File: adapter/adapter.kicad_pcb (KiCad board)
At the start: 2 copper layers, 61 x 25.4 mm, 4 parts, among them J1 FlipperGPIO, U1 CC1101_Connector

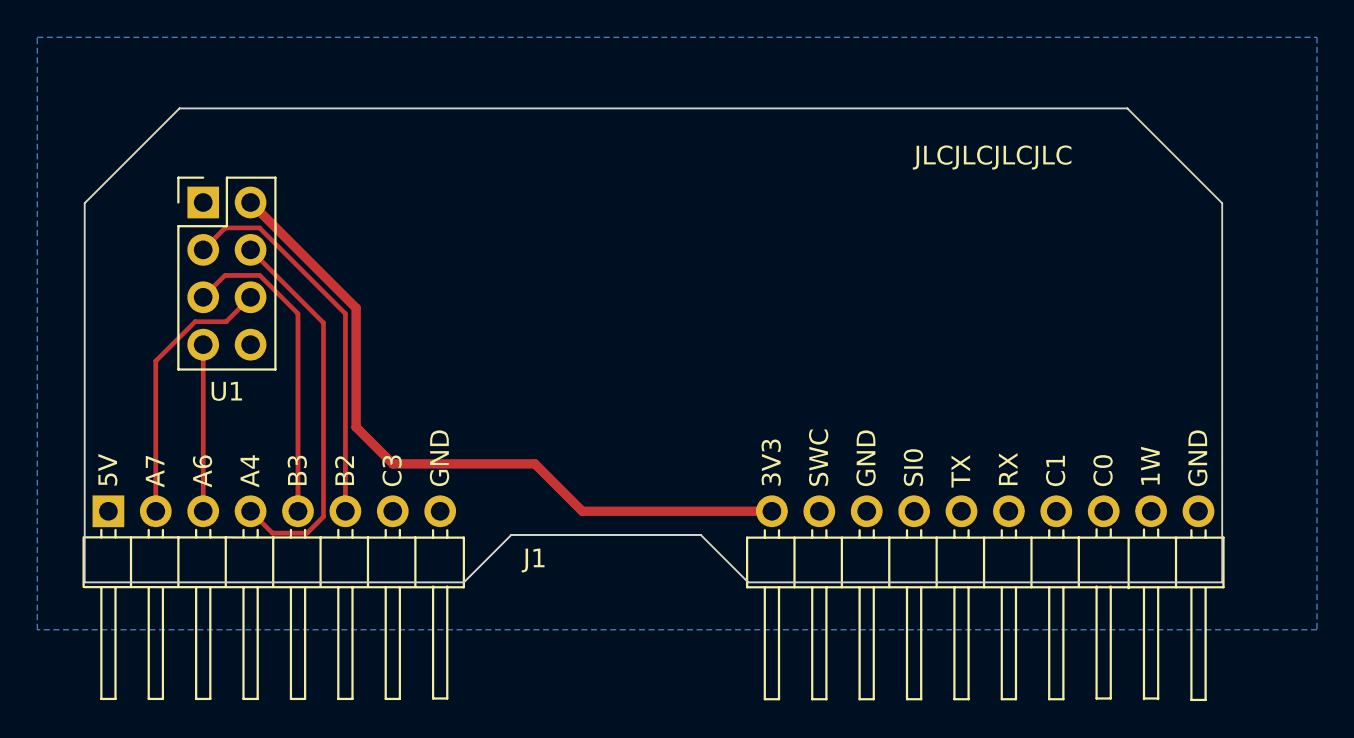
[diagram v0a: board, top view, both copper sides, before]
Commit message: include a 5V to 3.3V buck converter for more reliable power supply update to include a power LED since 5V is not always active
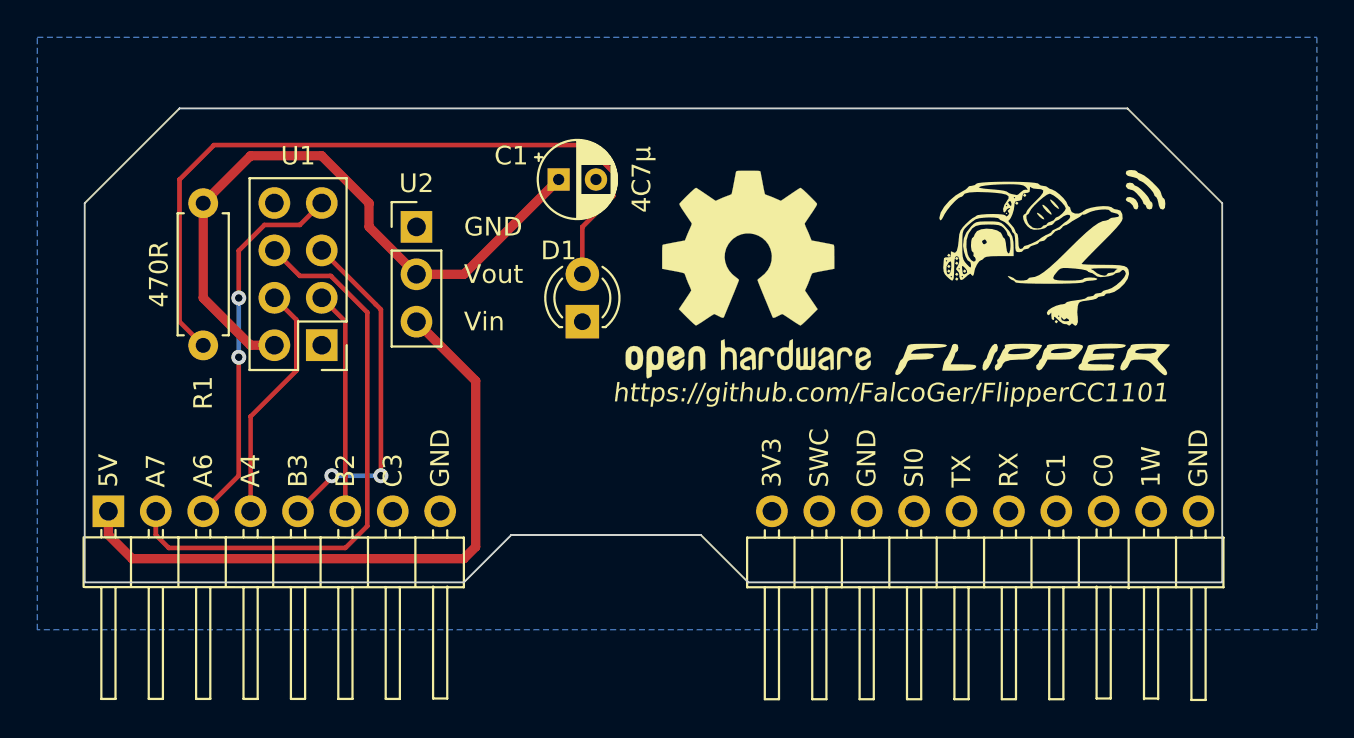
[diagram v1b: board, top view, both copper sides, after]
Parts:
- added C1: 4C7µ, Capacitor_THT:CP_Radial_D4.0mm_P2.00mm, F.Cu at (120.7, 83.8)
- added D1: LED, LED_THT:LED_D3.0mm, F.Cu at (121.9, 91.4)
- added R1: 470R, Resistor_THT:R_Axial_DIN0207_L6.3mm_D2.5mm_P7.62mm_Horizontal, F.Cu at (101.6, 85.1)
- added U2: AMS1117-3.3, Connector_PinHeader_2.54mm:PinHeader_1x03_P2.54mm_Vertical, F.Cu at (113.0, 86.4)
- REF** (x2): moved to F.Cu
- moved REF** 16.5 mm to (130.8, 88.9), turned to 0 degrees
- moved U1 9.94 mm to (108.0, 92.7), turned to 180 degrees
- moved REF** 8.89 mm to (146.1, 81.2), turned to 0 degrees
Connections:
- J1 pad 1: unconnected-(J1-Pad1) -> /5V
- J1 pad 5: /GDO0 -> /SCK
- J1 pad 6: Net-(U1-Pad3) -> /GDO0
- J1 pad 9: /3V3 -> unconnected-(J1-Pad9)
- U1 pad 3: Net-(U1-Pad3) -> /GDO0
- U1 pad 5: /GDO0 -> /SCK
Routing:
- net Net-(D1-Pad2): track 0.00 -> 40.2 mm
- net /5V: track 0.00 -> 35.1 mm
- net Net-(U1-Pad3): track 20.6 -> 0.00 mm
- net /SCK: track 0.00 -> 18.7 mm, vias 0 -> 2
- net /MOSI: track 14.5 -> 31.2 mm
- net /MISO: track 8.93 -> 20.3 mm, vias 0 -> 2
- net /CSN: track 20.7 -> 12.9 mm
- net /GDO0: track 17.0 -> 12.0 mm
- net /3V3: track 38.5 -> 35.5 mm
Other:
- board text added: "GND"
- board text added: "Vin"
- board text added: "Vout"

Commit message: rearranged board layout to make space for the buck converter
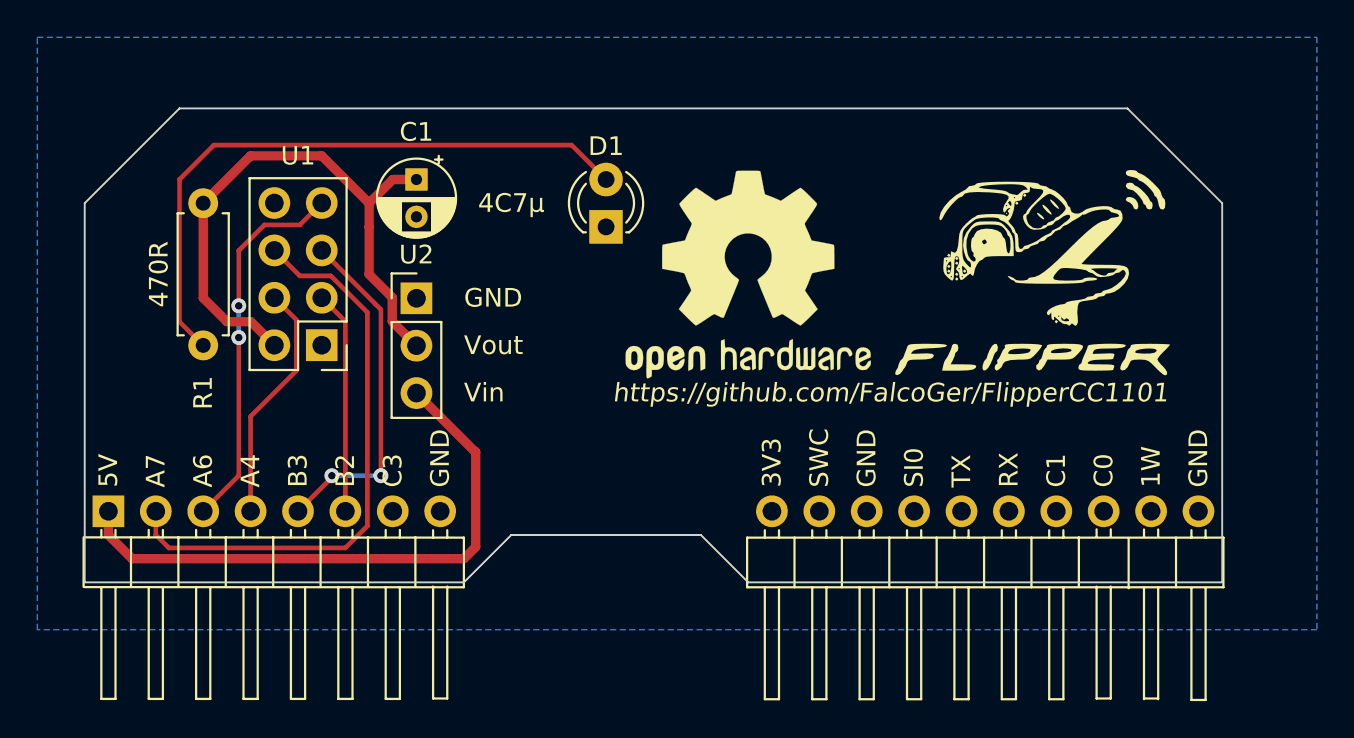
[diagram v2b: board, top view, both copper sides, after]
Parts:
- moved C1 7.62 mm to (113.0, 83.8), turned to -90 degrees
- moved D1 5.24 mm to (123.2, 86.4)
- moved U2 3.83 mm to (113.0, 90.2)
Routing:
- net Net-(D1-Pad2): track 40.2 -> 33.8 mm
- net /5V: track 35.1 -> 31.3 mm
- net /3V3: track 35.5 -> 32.7 mm
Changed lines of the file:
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@@
   )
   (footprint "Connector_PinHeader_2.54mm:PinHeader_1x03_P2.54mm_Vertical" (layer "F.Cu")
-    (at 113.03 86.36)
+    (at 113.03 90.185)
     (descr "Through hole straight pin header, 1x03, 2.54mm pitch, single row")
     (tags "Through hole pin header THT 1x03 2.54mm single row")
@@
   )
   (footprint "Capacitor_THT:CP_Radial_D4.0mm_P2.00mm" (layer "F.Cu")
-    (at 120.65 83.82)
+    (at 113.03 83.82 -90)
     (descr "CP, Radial series, Radial, pin pitch=2.00mm, , diameter=4mm, Electrolytic Capacitor")
     (tags "CP Radial series Radial pin pitch 2.00mm  diameter 4mm Electrolytic Capacitor")
@@
     (property "Sheetname" "")
     (attr through_hole)
-    (fp_text reference "C1" (at -2.54 -1.27) (layer "F.SilkS")
+    (fp_text reference "C1" (at -2.54 0 180) (layer "F.SilkS")
       (effects (font (size 1 1) (thickness 0.15)))
     )
-    (fp_text value "4C7µ" (at 4.445 0 90) (layer "F.SilkS")
+    (fp_text value "4C7µ" (at 1.27 -5.08) (layer "F.SilkS")
       (effects (font (size 1 1) (thickness 0.15)))
     )
-    (fp_text user "${REFERENCE}" (at 1 0) (layer "F.Fab")
+    (fp_text user "${REFERENCE}" (at 1 0 90) (layer "F.Fab")
       (effects (font (size 0.8 0.8) (thickness 0.12)))
     )
@@
     (fp_line (start -0.702554 -0.8675) (end -0.302554 -0.8675) (layer "F.Fab") (width 0.1))
     (fp_circle (center 1 0) (end 3 0) (layer "F.Fab") (width 0.1) (fill none))
-    (pad "1" thru_hole rect (at 0 0) (size 1.2 1.2) (drill 0.6) (layers *.Cu *.Mask)
+    (pad "1" thru_hole rect (at 0 0 270) (size 1.2 1.2) (drill 0.6) (layers *.Cu *.Mask)
       (net 17 "/3V3") (pintype "passive"))
-    (pad "2" thru_hole circle (at 2 0) (size 1.2 1.2) (drill 0.6) (layers *.Cu *.Mask)
+    (pad "2" thru_hole circle (at 2 0 270) (size 1.2 1.2) (drill 0.6) (layers *.Cu *.Mask)
       (net 16 "/GND") (pintype "passive"))
     (model "${KICAD6_3DMODEL_DIR}/Capacitor_THT.3dshapes/CP_Radial_D4.0mm_P2.00mm.wrl"
@@
   )
   (footprint "LED_THT:LED_D3.0mm" (layer "F.Cu")
-    (at 121.92 91.44 90)
+    (at 123.19 86.36 90)
     (descr "LED, diameter 3.0mm, 2 pins")
     (tags "LED diameter 3.0mm 2 pins")
@@
     (property "Sheetname" "")
     (attr through_hole)
-    (fp_text reference "D1" (at 3.81 -1.27 180) (layer "F.SilkS")
+    (fp_text reference "D1" (at 4.318 0 180) (layer "F.SilkS")
       (effects (font (size 1 1) (thickness 0.15)))
     )
@@
     (effects (font (size 1 1) (thickness 0.15)) (justify left mirror))
   )
-  (gr_text "GND" (at 115.57 86.36) (layer "F.SilkS")
+  (gr_text "GND" (at 115.57 90.17) (layer "F.SilkS")
     (effects (font (size 1 1) (thickness 0.15)) (justify left))
   )
-  (gr_text "Vout" (at 115.57 88.9) (layer "F.SilkS")
+  (gr_text "Vout" (at 115.57 92.71) (layer "F.SilkS")
     (effects (font (size 1 1) (thickness 0.15)) (justify left))
   )
@@
     (effects (font (size 1 1) (thickness 0.15) italic))
   )
-  (gr_text "Vin" (at 115.57 91.44) (layer "F.SilkS")
+  (gr_text "Vin" (at 115.57 95.25) (layer "F.SilkS")
     (effects (font (size 1 1) (thickness 0.15)) (justify left))
   )
-  (segment (start 121.92 88.9) (end 121.92 86.36) (width 0.25) (layer "F.Cu") (net 1))
+  (segment (start 121.345481 81.975481) (end 102.174519 81.975481) (width 0.25) (layer "F.Cu") (net 1))
+  (segment (start 100.33 83.82) (end 100.33 91.44) (width 0.25) (layer "F.Cu") (net 1))
   (segment (start 102.174519 81.975481) (end 100.33 83.82) (width 0.25) (layer "F.Cu") (net 1))
-  (segment (start 121.92 86.36) (end 123.574511 84.705489) (width 0.25) (layer "F.Cu") (net 1))
-  (segment (start 123.574511 84.705489) (end 123.574511 83.437054) (width 0.25) (layer "F.Cu") (net 1))
-  (segment (start 123.574511 83.437054) (end 122.112938 81.975481) (width 0.25) (layer "F.Cu") (net 1))
-  (segment (start 100.33 83.82) (end 100.33 91.44) (width 0.25) (layer "F.Cu") (net 1))
+  (segment (start 123.19 83.82) (end 121.345481 81.975481) (width 0.25) (layer "F.Cu") (net 1))
   (segment (start 100.33 91.44) (end 101.6 92.71) (width 0.25) (layer "F.Cu") (net 1))
-  (segment (start 122.112938 81.975481) (end 102.174519 81.975481) (width 0.25) (layer "F.Cu") (net 1))
-  (segment (start 116.205 94.615) (end 113.03 91.44) (width 0.5) (layer "F.Cu") (net 2))
   (segment (start 97.79 104.14) (end 115.57 104.14) (width 0.5) (layer "F.Cu") (net 2))
   (segment (start 96.52 101.6) (end 96.52 102.87) (width 0.5) (layer "F.Cu") (net 2))
+  (segment (start 116.205 103.505) (end 116.205 98.425) (width 0.5) (layer "F.Cu") (net 2))
   (segment (start 96.52 102.87) (end 97.79 104.14) (width 0.5) (layer "F.Cu") (net 2))
   (segment (start 115.57 104.14) (end 116.205 103.505) (width 0.5) (layer "F.Cu") (net 2))
-  (segment (start 116.205 103.505) (end 116.205 94.615) (width 0.5) (layer "F.Cu") (net 2))
+  (segment (start 116.19 98.425) (end 116.205 98.425) (width 0.5) (layer "F.Cu") (net 2))
+  (segment (start 113.03 95.265) (end 116.19 98.425) (width 0.5) (layer "F.Cu") (net 2))
   (segment (start 99.06 102.87) (end 99.06 101.6) (width 0.25) (layer "F.Cu") (net 12))
   (segment (start 110.394511 90.938501) (end 110.394511 102.390969) (width 0.25) (layer "F.Cu") (net 12))
@@
   (segment (start 110.394511 102.390969) (end 109.22 103.56548) (width 0.25) (layer "F.Cu") (net 12))
   (segment (start 109.22 103.56548) (end 99.75548 103.56548) (width 0.25) (layer "F.Cu") (net 12))
-  (segment (start 103.505 93.345) (end 103.505 99.695) (width 0.25) (layer "F.Cu") (net 13))
   (segment (start 103.505 99.695) (end 101.6 101.6) (width 0.25) (layer "F.Cu") (net 13))
   (segment (start 107.955 85.08) (end 106.780489 86.254511) (width 0.25) (layer "F.Cu") (net 13))
   (segment (start 106.780489 86.254511) (end 104.880489 86.254511) (width 0.25) (layer "F.Cu") (net 13))
-  (segment (start 103.505 87.63) (end 103.505 90.17) (width 0.25) (layer "F.Cu") (net 13))
+  (segment (start 103.505 92.2895) (end 103.505 99.695) (width 0.25) (layer "F.Cu") (net 13))
+  (segment (start 103.505 87.63) (end 103.505 90.5905) (width 0.25) (layer "F.Cu") (net 13))
   (segment (start 104.880489 86.254511) (end 103.505 87.63) (width 0.25) (layer "F.Cu") (net 13))
-  (via (at 103.505 93.345) (size 0.8) (drill 0.4) (layers "F.Cu" "B.Cu") (net 13))
-  (via (at 103.505 90.17) (size 0.8) (drill 0.4) (layers "F.Cu" "B.Cu") (net 13))
-  (segment (start 103.505 90.17) (end 103.505 93.345) (width 0.25) (layer "B.Cu") (net 13))
+  (via (at 103.505 90.5905) (size 0.8) (drill 0.4) (layers "F.Cu" "B.Cu") (net 13))
+  (via (at 103.505 92.2895) (size 0.8) (drill 0.4) (layers "F.Cu" "B.Cu") (net 13))
+  (segment (start 103.505 90.5905) (end 103.505 92.2895) (width 0.25) (layer "B.Cu") (net 13))
   (segment (start 104.14 96.52) (end 104.14 101.6) (width 0.25) (layer "F.Cu") (net 14))
   (segment (start 105.415 90.16) (end 106.589511 91.334511) (width 0.25) (layer "F.Cu") (net 14))
@@
   (segment (start 110.49 85.09) (end 110.49 86.36) (width 0.5) (layer "F.Cu") (net 17))
   (segment (start 107.95 82.55) (end 110.49 85.09) (width 0.5) (layer "F.Cu") (net 17))
-  (segment (start 101.6 90.17) (end 104.13 92.7) (width 0.5) (layer "F.Cu") (net 17))
-  (segment (start 113.03 88.9) (end 115.57 88.9) (width 0.5) (layer "F.Cu") (net 17))
-  (segment (start 110.49 86.36) (end 113.03 88.9) (width 0.5) (layer "F.Cu") (net 17))
-  (segment (start 115.57 88.9) (end 120.65 83.82) (width 0.5) (layer "F.Cu") (net 17))
+  (segment (start 111.730489 91.425489) (end 111.730489 90.140489) (width 0.5) (layer "F.Cu") (net 17))
+  (segment (start 104.155 91.44) (end 102.87 91.44) (width 0.5) (layer "F.Cu") (net 17))
+  (segment (start 105.415 92.7) (end 104.155 91.44) (width 0.5) (layer "F.Cu") (net 17))
   (segment (start 101.6 85.09) (end 104.14 82.55) (width 0.5) (layer "F.Cu") (net 17))
-  (segment (start 101.6 85.09) (end 101.6 90.17) (width 0.5) (layer "F.Cu") (net 17))
-  (segment (start 104.13 92.7) (end 105.415 92.7) (width 0.5) (layer "F.Cu") (net 17))
+  (segment (start 111.76 83.82) (end 113.03 83.82) (width 0.5) (layer "F.Cu") (net 17))
+  (segment (start 102.87 91.44) (end 101.6 90.17) (width 0.5) (layer "F.Cu") (net 17))
+  (segment (start 110.49 88.9) (end 110.49 86.36) (width 0.5) (layer "F.Cu") (net 17))
+  (segment (start 110.49 85.09) (end 111.76 83.82) (width 0.5) (layer "F.Cu") (net 17))
+  (segment (start 101.6 90.17) (end 101.6 85.09) (width 0.5) (layer "F.Cu") (net 17))
+  (segment (start 113.03 92.725) (end 111.730489 91.425489) (width 0.5) (layer "F.Cu") (net 17))
+  (segment (start 111.730489 90.140489) (end 110.49 88.9) (width 0.5) (layer "F.Cu") (net 17))
   (segment (start 104.14 82.55) (end 107.95 82.55) (width 0.5) (layer "F.Cu") (net 17))
   (segment (start 108.4955 99.695) (end 108.4955 99.7845) (width 0.25) (layer "F.Cu") (net 18))

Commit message: slightly increase board size to clear PCB checker errors.
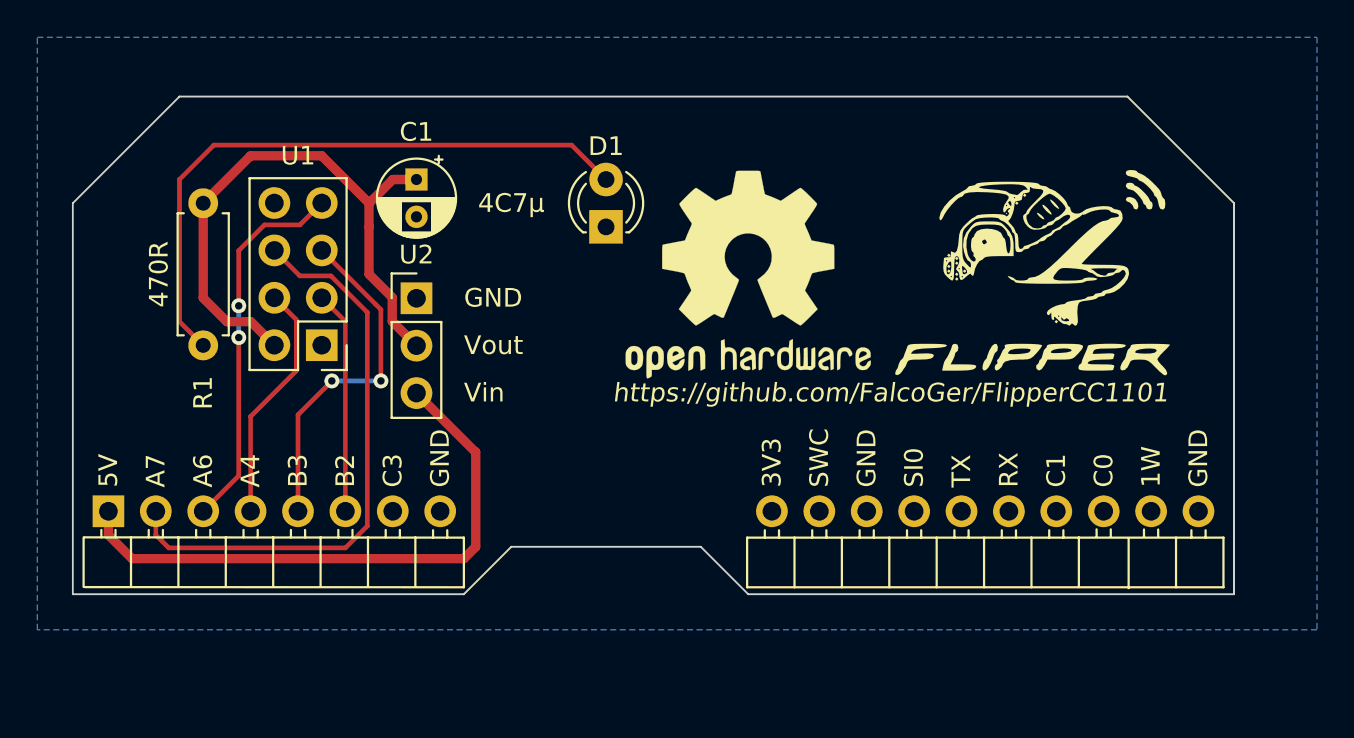
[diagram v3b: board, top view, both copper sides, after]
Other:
- board size 61 x 25.4 mm -> 62.2 x 26.7 mm
